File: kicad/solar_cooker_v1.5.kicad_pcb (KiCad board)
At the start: 2 copper layers, 152.7 x 77.2 mm, 20 parts, among them J1 Pt100, J2 microSD, J3 clock_module, J4 Pt100, J5 BME680, J6 GPS, J7 Pt100, J8 display, U1 anemometer, U2 AM2315C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

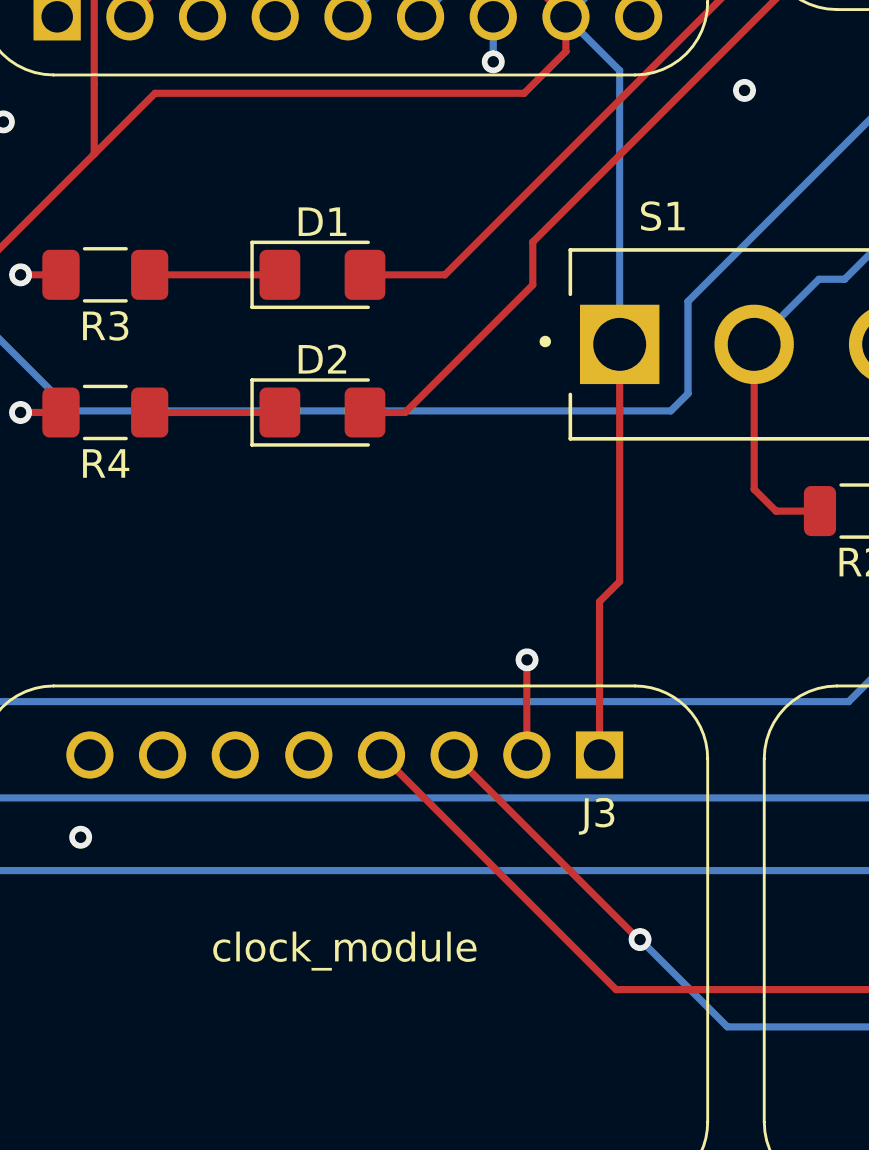
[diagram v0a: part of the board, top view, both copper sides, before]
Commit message: minor silkscreen fix
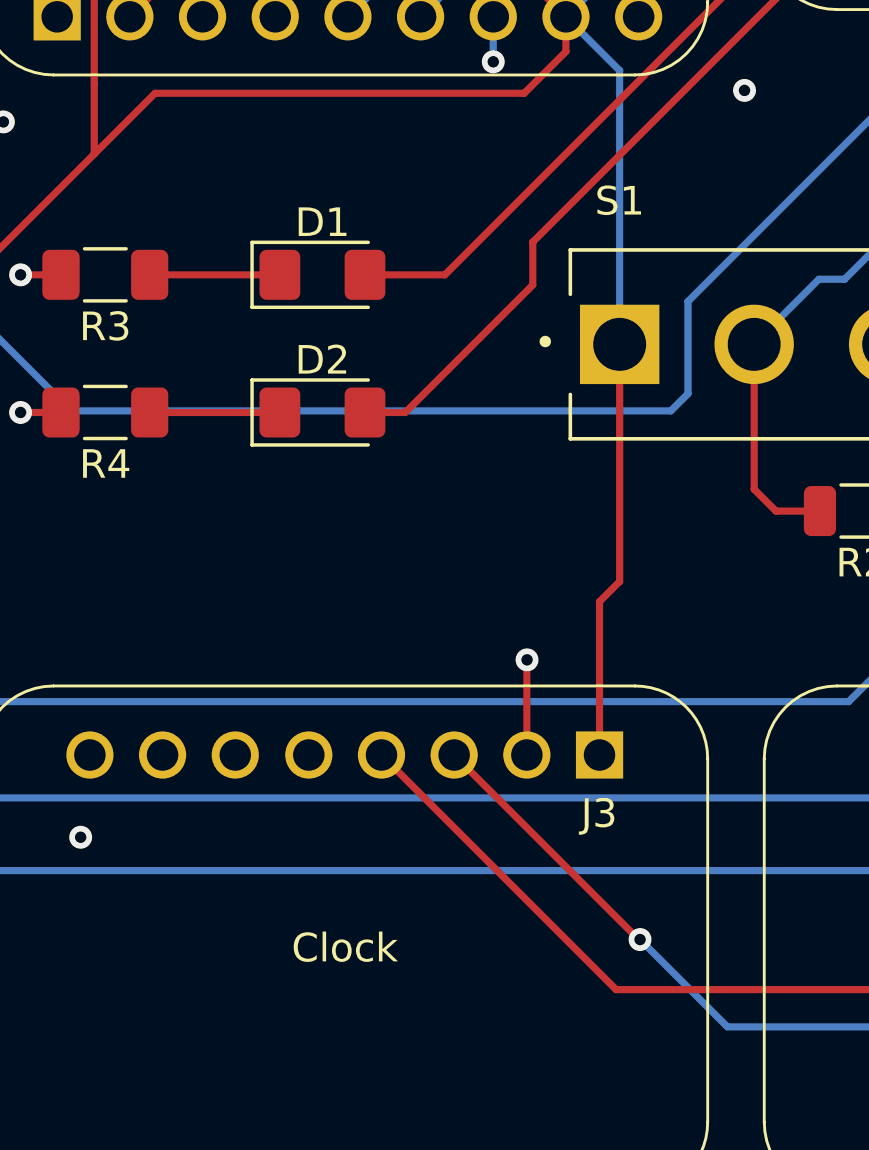
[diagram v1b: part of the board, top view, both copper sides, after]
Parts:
- J3: value clock_module -> Clock
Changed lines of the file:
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@@
     (pad "7" thru_hole circle (at -7.62 -6.35) (size 1.65 1.65) (drill 1.1) (layers "*.Cu" "*.Mask")
       (net 13 "/D6") (pinfunction "CS") (pintype "input"))
-    (group "" (id bf29318a-9556-4dc2-9d61-cdc7ddff67f1)
-      (members
-        046d1731-f1b9-4601-a2a1-ae788f2c99bc
-        0ad049b8-7dcd-4bf0-a96c-e8f50517e3d7
-        20f1db34-6875-4022-b06a-1227d99c6c6b
-        3020c44f-e6ee-4d6a-88fa-f33302537ece
-        a750689a-3667-48c7-ba15-56e9a78512ca
-        a8af9359-0f7c-40fc-bd90-a5a4aaaa3224
-        aca174ba-0e48-442a-9768-43916582ad32
-      )
+    (group "" (id 5401e7ee-6c69-4c9d-a56d-368ab4bcb0ce)
+      (members
+        0ccf488b-a217-48bb-9251-0c343f802538
+        0e64d26e-d068-491d-a1fe-60d2b3884a42
+        1b630fef-a978-4b08-874b-a3d4b45b76ff
+        4e9e00aa-b808-478a-ae15-09d42b36de30
+        57388b8d-f2d3-49bf-bf4a-0340727b5296
+        ccb002f8-50a1-4b01-9225-ca9f18f7068b
+        ef31efd0-e5a1-4ad2-a537-8647005f7d07
+      )
+    )
+    (model "${KIPRJMOD}/library/SSQ-107-01-G-S/SSQ-107-01-G-S.step"
+      (offset (xyz 0 6.35 0))
+      (scale (xyz 1 1 1))
+      (rotate (xyz -90 0 0))
     )
   )
@@
     (property "Supplier" "Digi-Key")
     (attr through_hole)
-    (fp_text reference "S1" (at -3.175 -4.445) (layer "F.SilkS")
+    (fp_text reference "S1" (at -4.7 -5) (layer "F.SilkS")
         (effects (font (size 1 1) (thickness 0.15)))
     )
@@
         (effects (font (size 1 1) (thickness 0.15)))
     )
-    (fp_text value "clock_module" (at 0 0 unlocked) (layer "F.SilkS")
+    (fp_text value "Clock" (at 0 0 unlocked) (layer "F.SilkS")
         (effects (font (size 1 1) (thickness 0.15)))
     )
@@
     (pad "8" thru_hole circle (at -8.908051 -6.749051) (size 1.65 1.65) (drill 1.1) (layers "*.Cu" "*.Mask")
       (net 104 "unconnected-(J3-RST-Pad8)") (pinfunction "RST") (pintype "input+no_connect"))
-    (group "" (id b405675c-1503-46df-8095-b4ea8e32c93b)
-      (members
-        0c137e68-8d30-4896-9ac1-06d00b1f9d90
-        240000d7-1584-41f5-9120-fe9e6390fa84
-        4286da84-15d7-4aff-9703-023da1cc966d
-        4c3e2391-a0e2-47f9-a390-fdb7892d7b66
-        68d1fac1-e5d4-4266-87fd-47d60792933c
-        71ed6dee-599f-40dd-a4bf-a709f96cc17b
-        833b3d1b-c015-4356-97b5-c2534c70832d
-        f11edabd-db53-4b46-9aa5-123d8878a2b7
-      )
-    )
+    (group "" (id 85f703f6-4ab7-4c24-b191-c366a717c7fa)
+      (members
+        24d83e1f-ba48-4f3d-884c-bdf2eb21c5cd
+        41542246-2c90-4183-9759-5b494edfb522
+        94656c2d-818f-48bd-bd16-b16a3cad3300
+        9d7c1538-209e-4fc3-91f4-7e6721154bfc
+        a3b7a720-7d8c-4698-8514-348418660ec6
+        af246e1a-2a86-4548-b053-d44dbcd9e7eb
+        db019186-d298-4dcb-8d79-3aa18c3496a2
+        ee47ea27-6b1f-4e60-a8fe-437c55e1326f
+      )
+    )
